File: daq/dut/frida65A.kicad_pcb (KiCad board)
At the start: 4 copper layers, 100 x 100 mm, 98 parts, among them J1 SMA Molex 733910070, J2 SMA Molex 733910070, J3 SMA Molex 733910070, J4 RJ45 Molex 446200002, J5 DisplayPort Molex 472720024, J6 MiniFitJr Molex 469990014, J7 Conn_02x06_Odd_Even, Q1 NMOS, U1 ASIC FRIDA 65A, U2 LevelShifter TI TXV0106Q1, U3 DiffAmp TI THS4541

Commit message: Leaf device generation, docs on layout proto, rules/dimension proto, and constraints proto
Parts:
- added C31: 100n, Capacitor_SMD:C_0402_1005Metric, F.Cu at (4.99, 0.48)
- added C32: 1u, Capacitor_SMD:C_0402_1005Metric, F.Cu at (4.99, 2.46)
- added C33: 51pF, Capacitor_SMD:C_0402_1005Metric, F.Cu at (4.99, 4.42)
- added C34: 51pF, Capacitor_SMD:C_0402_1005Metric, F.Cu at (4.99, 6.39)
- added G***: LOGO, frida:SiLab Logo, F.Cu at (102.8, 100.4)
- added G***: LOGO, frida:UBonn Logo, F.Cu at (102.8, 92.8)
- added REF**: FTD_Logo, frida:FTD_Logo, F.Cu at (107.6, 65.4)
- added REF**: Layer_count, frida:Layer_count, F.Cu at (107.2, 107.2)
- moved TP15 197.1 mm to (1.52, 1.52)
- moved TP16 193.4 mm to (1.52, 5.58)
- moved TP19 191.1 mm to (1.52, 17.7)
- moved TP17 190.0 mm to (1.52, 9.62)
- moved TP18 186.8 mm to (1.52, 13.7)
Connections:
- D1 pad 2: /VDD_IO -> /VDD_DAC
- D1 pad 3: Net-(U3-IN+) -> unconnected-(D1-K-Pad3)
- D2 pad 2: /VDD_IO -> /VDD_DAC
- D2 pad 3: Net-(U3-IN-) -> unconnected-(D2-K-Pad3)
- J4 pad 7: /VDD_DAQ -> /VDD_BDAQ
- J4 pad 8: unconnected-(J4-Pad8) -> /VDD_BDAQ
- J5 pad 1: /CLK_LOGIC_N -> /CLK_COMP_P
- J5 pad 10: /CLK_INIT_N -> /CLK_SAMP_N
- J5 pad 12: /CLK_INIT_P -> /CLK_SAMP_P
- J5 pad 15: /COMP_OUT_P -> /CLK_INIT_N
- J5 pad 17: /COMP_OUT_N -> /CLK_INIT_P
- J5 pad 3: /CLK_LOGIC_P -> /CLK_COMP_N
- J5 pad 4: /CLK_COMP_N -> /CLK_LOGIC_P
- J5 pad 6: /CLK_COMP_P -> /CLK_LOGIC_N
- J5 pad 7: /CLK_SAMP_N -> /COMP_OUT_N
- J5 pad 9: /CLK_SAMP_P -> /COMP_OUT_P
- R1 pad 1: /CLK_LOGIC_N -> /CLK_COMP_P
- R1 pad 2: /CLK_LOGIC_P -> /CLK_COMP_N
- R2 pad 1: /CLK_COMP_N -> /CLK_LOGIC_P
- R2 pad 2: /CLK_COMP_P -> /CLK_LOGIC_N
- R20 pad 2: /VDD_IO -> /VDD_DAC
- R5 pad 1: /CLK_LOGIC_N -> /CLK_COMP_P
- R6 pad 1: /CLK_LOGIC_P -> /CLK_COMP_N
- R7 pad 1: /CLK_COMP_N -> /CLK_LOGIC_P
- R8 pad 1: /CLK_COMP_P -> /CLK_LOGIC_N
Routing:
- net /VDD_IO: track 107.2 -> 75.8 mm
- net /CLK_COMP_N: track 69.5 -> 50.4 mm
- net /CLK_COMP_P: track 69.5 -> 55.1 mm
- net /SPI_CS_B: track 53.6 -> 42.2 mm, vias 3 -> 2
- net /COMP_OUT_P: track 65.4 -> 54.3 mm, vias 2 -> 0
- net /COMP_OUT_N: track 65.4 -> 54.3 mm, vias 2 -> 0
- net /CLK_LOGIC_N: track 75.1 -> 64.2 mm
- net /CLK_LOGIC_P: track 75.1 -> 64.7 mm
- net /SPI_SCLK: track 48.4 -> 40.6 mm, vias 3 -> 2
- net /SPI_SDO: track 51.0 -> 43.6 mm, vias 3 -> 2
- net Net-(J5-Pad13): track 7.41 -> 0.00 mm
- net Net-(J5-Pad14): track 6.46 -> 0.00 mm
- net /RST_B: track 49.4 -> 45.4 mm, vias 3 -> 2
- net GND: track 54.4 -> 50.9 mm, vias 45 -> 44
- net /SPI_SDI: track 49.3 -> 47.3 mm, vias 3 -> 2
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
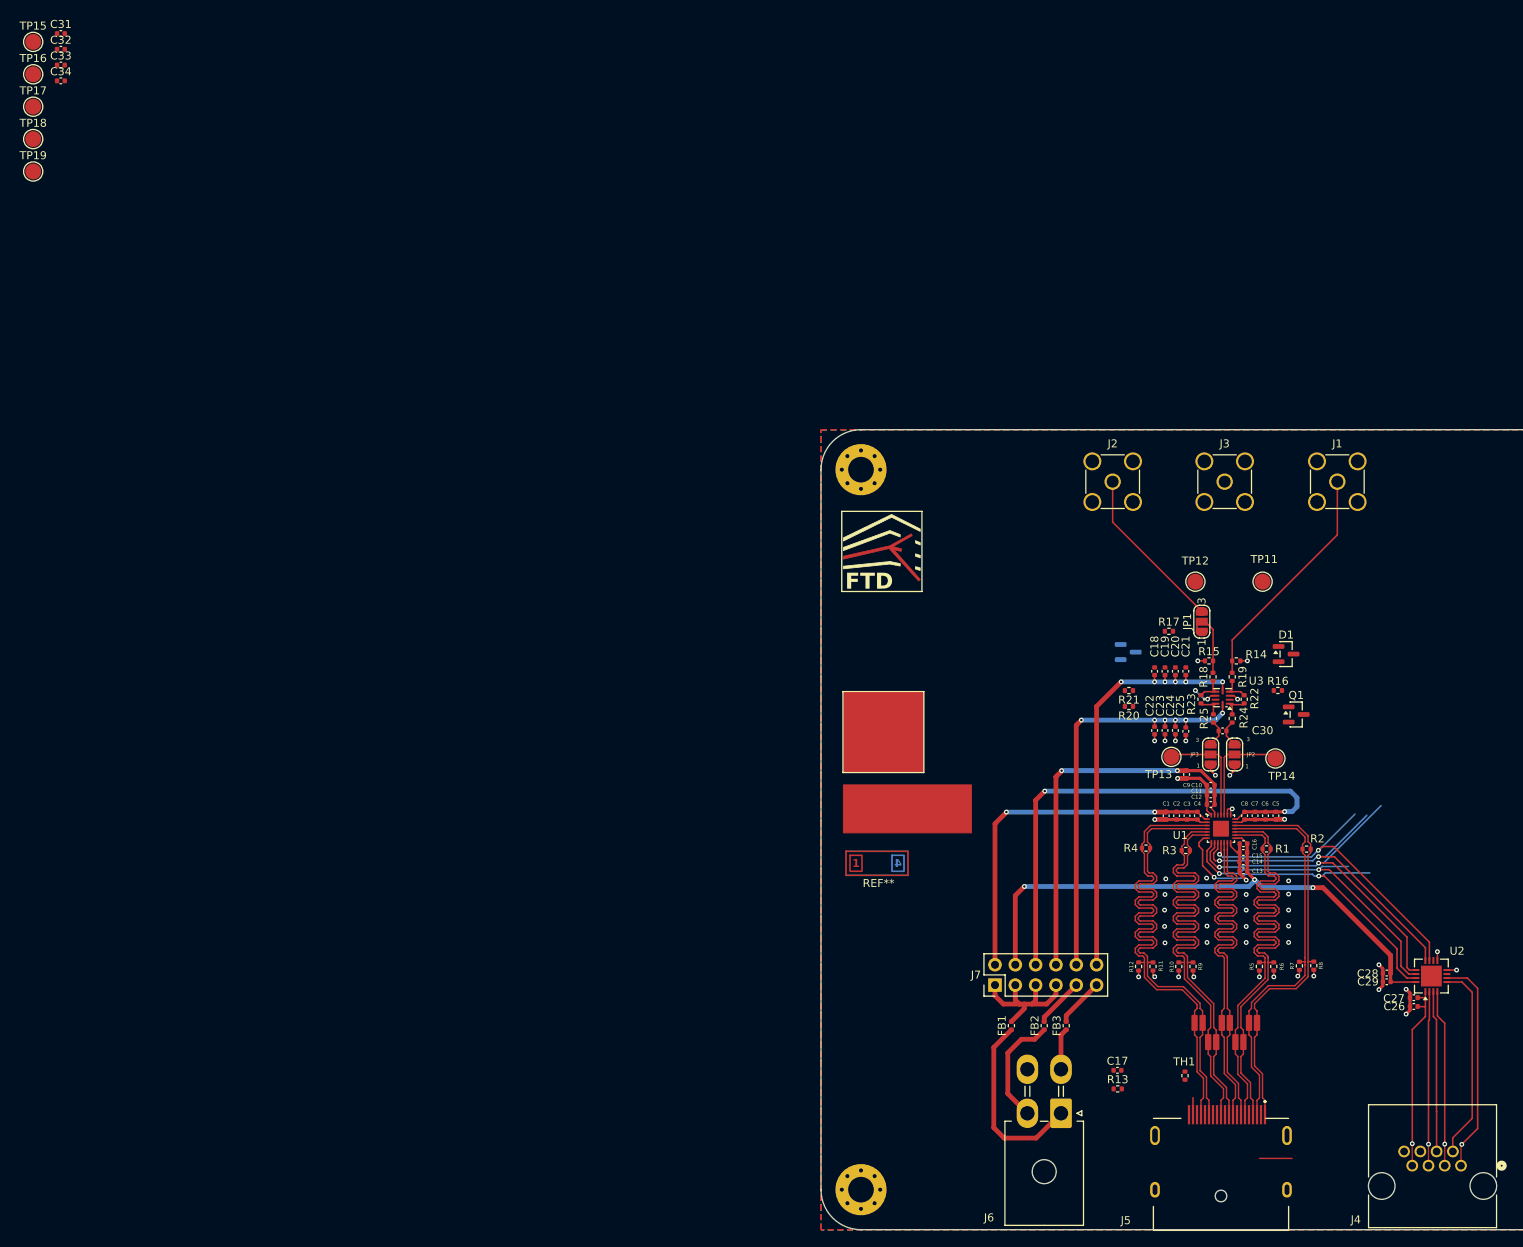
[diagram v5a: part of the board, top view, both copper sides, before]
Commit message: Add pcb decal
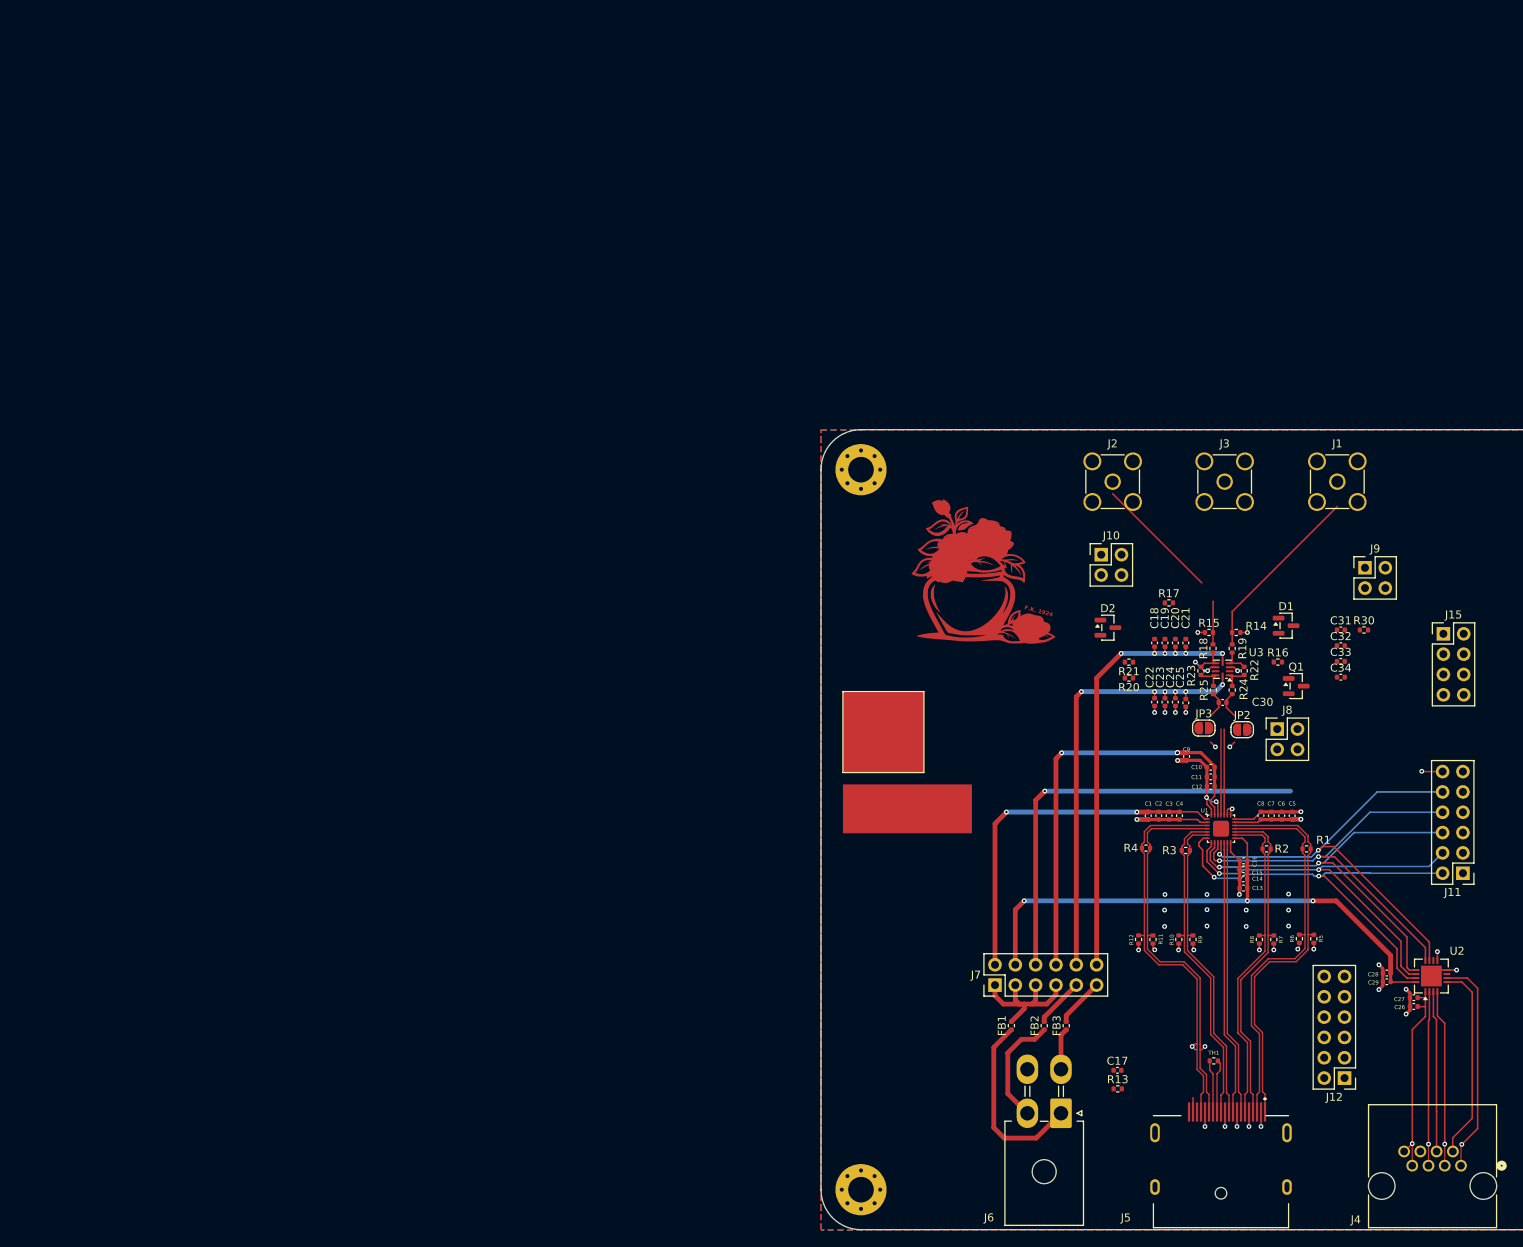
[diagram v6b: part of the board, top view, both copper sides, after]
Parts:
- removed JP1: SolderJumper_3_Open, Jumper:SolderJumper-3_P1.3mm_Open_RoundedPad1.0x1.5mm_NumberLabels
- removed REF**: FTD_Logo, frida:FTD_Logo
- removed REF**: Layer_count, frida:Layer_count
- removed TP1, TP10, TP2, TP3, TP4, TP5, TP6, TP7, TP8, TP9: TestPoint Keystone 5001, frida:Test_Point
- removed TP11, TP12, TP13, TP14, TP15, TP16, TP17, TP18, TP19: TestPoint, TestPoint:TestPoint_Pad_D2.0mm
- added G***: LOGO, frida:final, F.Cu at (119.6, 70.7)
- added J10: CFG VIN_EXT, Connector_PinHeader_2.54mm:PinHeader_2x02_P2.54mm_Vertical, F.Cu at (135.0, 65.6)
- added J11: SPI TP, Connector_PinHeader_2.54mm:PinHeader_2x06_P2.54mm_Vertical, F.Cu at (180.2, 105.4)
- added J12: TP CLOCKS, Connector_PinHeader_2.54mm:PinHeader_2x06_P2.54mm_Vertical, F.Cu at (165.4, 131.1)
- added J15: TP AMP, Connector_PinHeader_2.54mm:PinHeader_2x04_P2.54mm_Vertical, F.Cu at (177.8, 75.5)
- added J8: CFG VIN_P, Connector_PinHeader_2.54mm:PinHeader_2x02_P2.54mm_Vertical, F.Cu at (157.0, 87.4)
- added J9: CFG VIN_P, Connector_PinHeader_2.54mm:PinHeader_2x02_P2.54mm_Vertical, F.Cu at (168.0, 67.3)
- added R30: 10k, Resistor_SMD:R_0402_1005Metric, F.Cu at (167.9, 75.0)
- D2: moved to F.Cu
- J7: value Conn_02x06_Odd_Even -> POWER
- JP2, JP3: value SolderJumper_3_Open -> CFG CLAMP; footprint Jumper:SolderJumper-3_P1.3mm_Open_RoundedPad1.0x1.5mm_NumberLabels -> Jumper:SolderJumper-2_P1.3mm_Open_RoundedPad1.0x1.5mm
- Q1: value NMOS -> Q_PMOS_DGS
- moved C31 176.5 mm to (165.0, 75.0)
- moved C32 176.5 mm to (165.0, 77.0)
- moved C33 176.5 mm to (165.0, 79.0)
- moved C34 176.5 mm to (165.0, 80.9)
- moved R5 7.63 mm to (161.6, 113.6)
- moved R8 7.55 mm to (154.8, 113.7)
- moved R2 5.00 mm to (155.7, 102.4), turned to 180 degrees
- moved R1 5.00 mm to (160.7, 102.4), turned to 180 degrees
- moved R6 4.72 mm to (159.8, 113.6)
- moved R7 4.59 mm to (156.6, 113.7)
- moved TH1 4.05 mm to (149.1, 128.9), turned to 180 degrees
- moved D2 3.97 mm to (135.9, 74.8)
- moved C30 3.55 mm to (150.2, 84.1)
- moved R14 3.55 mm to (151.9, 75.3)
- moved R15 3.55 mm to (148.5, 75.3)
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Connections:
- net /AMP_EN_EXT_B renamed /AMP_PD_EXT
- C26 pad 1: /VDD_DAQ -> /VDD_BDAQ
- C27 pad 1: /VDD_DAQ -> /VDD_BDAQ
- C30 pad 1: Net-(JP2-B) -> Net-(J8-Pin_3)
- C30 pad 2: Net-(JP3-B) -> Net-(J9-Pin_1)
- D1 pad 3: unconnected-(D1-K-Pad3) -> Net-(JP2-A)
- D2 pad 3: unconnected-(D2-K-Pad3) -> Net-(JP3-B)
- J5 pad 19: /VDD_IO -> /VDD
- JP2 pad 1: /VIN_N_EXT -> Net-(JP2-A)
- JP3 pad 1: /VIN_P_EXT -> /VIN_P
- JP3 pad 2: /VIN_P -> Net-(JP3-B)
- Q1 pad 1: /AMP_EN -> /AMP_PD_N
- Q1 pad 3: GND -> /VDD_DAC
- R16 pad 1: /VS_P -> /AMP_PD_N
- R16 pad 2: /AMP_EN -> /VS_N
- R24 pad 1: Net-(JP2-B) -> Net-(J8-Pin_3)
- R25 pad 1: Net-(JP3-B) -> Net-(J9-Pin_1)
- U2 pad 1: /VDD_DAQ -> /VDD_BDAQ
- U3 pad 3: /AMP_EN -> /AMP_PD_N
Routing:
- net GND: track 50.9 -> 91.1 mm
- net /CLK_SAMP_N: track 66.5 -> 40.2 mm
- net /CLK_SAMP_P: track 67.2 -> 40.8 mm
- net /VDD_BDAQ: track 0.00 -> 25.8 mm, vias 0 -> 1
- net /VDD_DAQ: track 24.4 -> 0.00 mm, vias 1 -> 0
- net /CLK_LOGIC_P: track 64.7 -> 42.2 mm
- net /CLK_LOGIC_N: track 64.2 -> 41.6 mm
- net /VIN_N_EXT: track 22.4 -> 0.85 mm
- net /COMP_OUT_N: track 54.3 -> 34.8 mm
- net /COMP_OUT_P: track 54.3 -> 34.8 mm
- net /CLK_INIT_N: track 68.0 -> 49.6 mm, vias 0 -> 1
- net /CLK_INIT_P: track 68.7 -> 51.0 mm, vias 0 -> 1
- net /SPI_SCLK: track 40.6 -> 53.1 mm
- net /SPI_CS_B: track 42.2 -> 54.3 mm
- net /SPI_SDO: track 43.6 -> 53.2 mm
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
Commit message: Schematic TODOs complete
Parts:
- R10, R11, R12, R5, R6, R7, R8, R9: value 10k -> 1k
- moved J12 11.2 mm to (176.3, 128.2), turned to -90 degrees
- moved C1 1.27 mm to (140.9, 97.0)
- moved C2 1.27 mm to (142.2, 97.0)
- moved C3 1.27 mm to (143.5, 97.0)
- moved C4 1.27 mm to (144.8, 97.0)
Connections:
- H1 pad 1: Earth -> unconnected-(H1-Pad1)_8
- H2 pad 1: Earth -> unconnected-(H2-Pad1)_8
- H3 pad 1: Earth -> unconnected-(H3-Pad1)_8
- H4 pad 1: Earth -> unconnected-(H4-Pad1)_8
- J4 pad 7: /VDD_BDAQ -> GND
- Q1 pad 3: /VDD_DAC -> /VDD_BDAQ
- U1 pad 29: (no net) -> GND
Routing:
- net GND: track 91.1 -> 99.8 mm
- net /VDD_A: track 45.2 -> 47.0 mm
